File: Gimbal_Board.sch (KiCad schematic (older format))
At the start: 21 parts, among them U1 TM4C129E_Launchpad

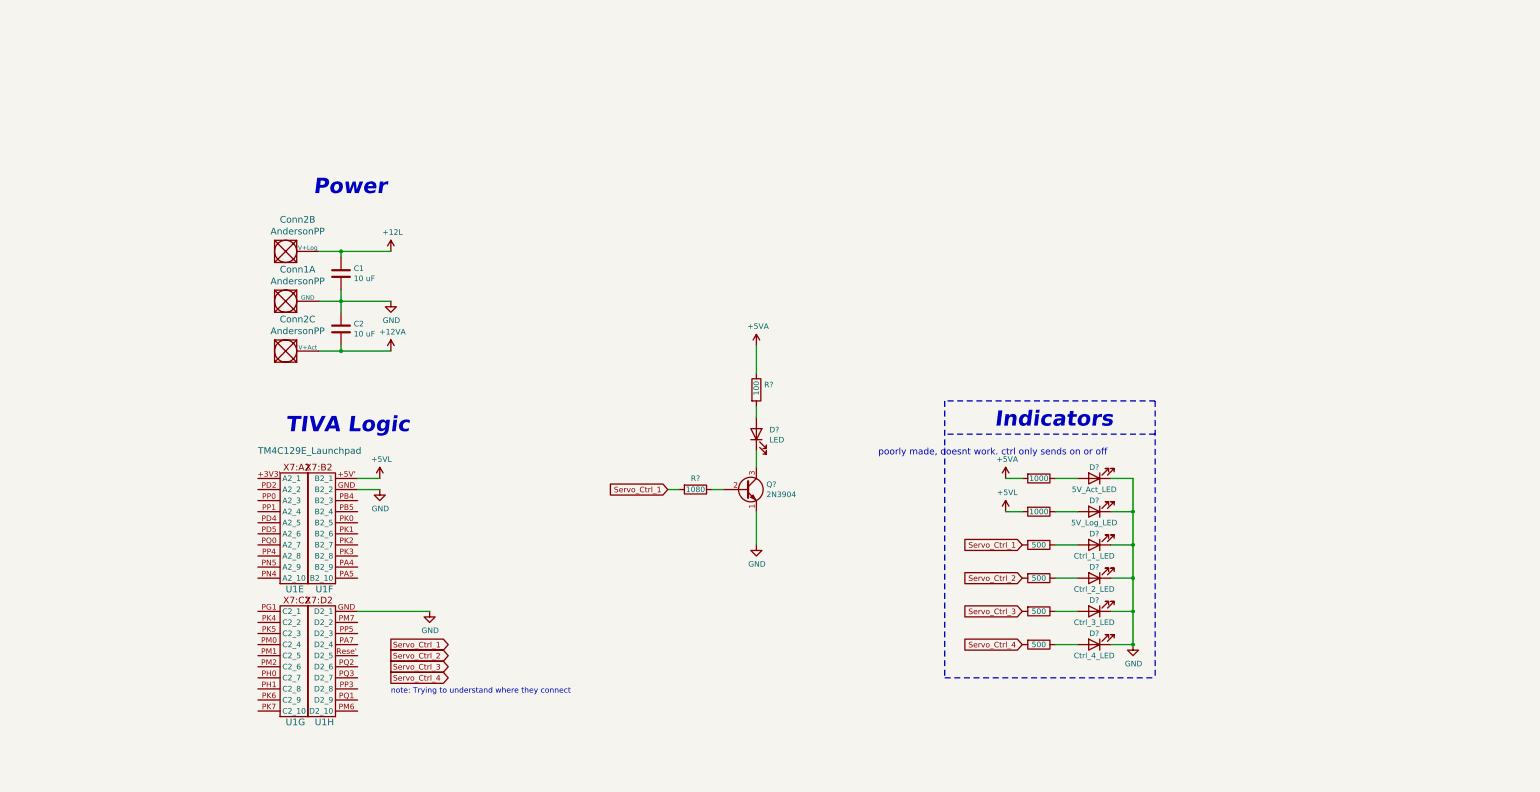
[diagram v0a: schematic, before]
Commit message: Schematic additions
Status of each section is located at the top of the schematic. Added the much of the designs from last year.  Used the updated indicator design (needs to be looked over). Tiva Logic needs to be looked at.
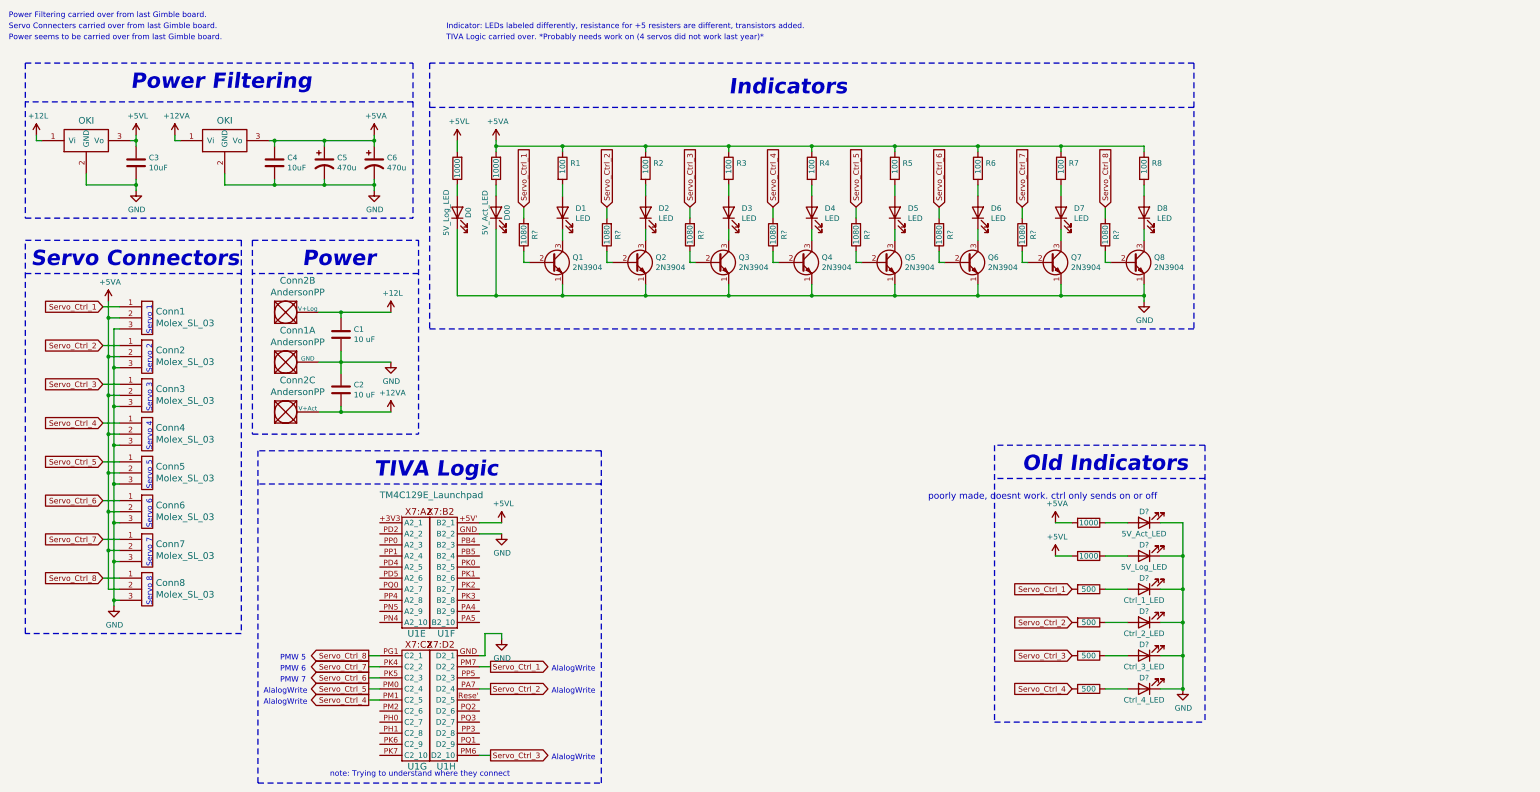
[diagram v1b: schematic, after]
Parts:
- added C3, C4: 10uF, symbol Device:C
- added C5, C6: 470u, symbol Device:CP1
- added Conn1, Conn3, Conn4, Conn5, Conn6, Conn7, Conn8: Molex_SL_03, symbol MRDT_Connectors:Molex_SL_03
- added unit 1 of Conn2
- added D0: 5V_Log_LED, symbol Device:LED
- added D00: 5V_Act_LED, symbol Device:LED
- added D2, D3, D4, D5, D6, D7, D8: LED, symbol Device:LED
- added Q2, Q3, Q4, Q5, Q6, Q7, Q8: 2N3904, Package_TO_SOT_THT:TO-92_Inline, symbol Transistor_BJT:2N3904
- added R2, R3, R4, R5, R6, R7, R8: 100, symbol Device:R
- added R? (x7): 1080, symbol Device:R
- added R? (x2): 1000, symbol Device:R
- added U? (x2): OKI, symbol MRDT_Devices:OKI
- gave numbers to parts that had none: 3
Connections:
- net +12L: now also U?.1 (Vi)
- net +12VA: now also U?.1 (Vi)
- net +5VA: now also C4.1, C5.1, C6.1, Conn1.2, Conn2.2, Conn3.2, Conn4.2, Conn5.2, Conn6.2, Conn7.2, Conn8.2, R2.1, R3.1, R4.1, R5.1, R6.1, R7.1, R8.1, R?.2, U?.3 (Vo)
- net +5VL: now also C3.1, R?.2, U?.3 (Vo)
- net GND: now also C3.2, C4.2, C5.2, C6.2, Conn1.3, Conn2.3, Conn3.3, Conn4.3, Conn5.3, Conn6.3, Conn7.3, Conn8.3, D0.1 (K), D00.1 (K), Q2.1 (E), Q3.1 (E), Q4.1 (E), Q5.1 (E), Q6.1 (E), Q7.1 (E), Q8.1 (E), U?.2 (GND), U?.2 (GND)
- net Servo_Ctrl_1: now also U1.PM7 (D2_2), Conn1.1
- net Servo_Ctrl_2: now also U1.PA7 (D2_4), Conn2.1, R?.2
- net Servo_Ctrl_3: now also U1.PM6 (D2_10), Conn3.1, R?.2
- net Servo_Ctrl_4: now also U1.PM1 (C2_5), Conn4.1, R?.2
- net Servo_Ctrl_8: now reaches U1.PG1 (C2_1)
- net Servo_Ctrl_8: now also Conn8.1, R?.2
- net Servo_Ctrl_7: now reaches U1.PK4 (C2_2)
- net Servo_Ctrl_7: now also Conn7.1, R?.2
- net Servo_Ctrl_6: now reaches U1.PK5 (C2_3)
- net Servo_Ctrl_6: now also Conn6.1, R?.2
- net Servo_Ctrl_5: now reaches U1.PM0 (C2_4)
- net Servo_Ctrl_5: now also Conn5.1, R?.2
- new net: Q2.2 (B), R?.1
- new net: D2.1 (K), Q2.3 (C)
- new net: D2.2 (A), R2.2
- new net: Q3.2 (B), R?.1
- new net: D3.1 (K), Q3.3 (C)
- new net: D3.2 (A), R3.2
- new net: Q4.2 (B), R?.1
- new net: D4.1 (K), Q4.3 (C)
- new net: D4.2 (A), R4.2
- new net: D00.2 (A), R?.1
- new net: D0.2 (A), R?.1
- new net: Q5.2 (B), R?.1
- new net: D5.1 (K), Q5.3 (C)
- new net: D5.2 (A), R5.2
- new net: Q6.2 (B), R?.1
- new net: D6.1 (K), Q6.3 (C)
- new net: D6.2 (A), R6.2
- new net: Q7.2 (B), R?.1
- new net: D7.1 (K), Q7.3 (C)
- new net: D7.2 (A), R7.2
- new net: Q8.2 (B), R?.1
- new net: D8.1 (K), Q8.3 (C)
- new net: D8.2 (A), R8.2
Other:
- note added: "AlalogWrite"
- note added: "Indicator: LEDs labeled differently, resistance for +5 resisters are different, transistors added.\n"
- note added: "Old Indicators"
- note added: "PMW 5"
- note added: "PMW 6"
- note added: "PMW 7"
- note added: "Power Filtering"
- note added: "Power Filtering carried over from last Gimble board."
- note added: "Power seems to be carried over from last Gimble board."
- note added: "Servo 1"
- note added: "Servo 2"
- note added: "Servo 3"
- note added: "Servo 4"
- note added: "Servo 5"
- note added: "Servo 6"
- note added: "Servo 7"
- note added: "Servo 8"
- note added: "Servo Connecters carried over from last Gimble board."
- note added: "Servo Connectors"
- note added: "TIVA Logic carried over. *Probably needs work on (4 servos did not work last year)*"
- moved on the sheet: C1, C2, Conn1A, Conn2B, Conn2C, D1, D?, Q1, R1, R?, U1E, U1F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

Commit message: 6 Servo Changes
Changed to be 6 servos. Pins should be looked over. (Old Indicators should be deleted if no one needs it for reference on this file).
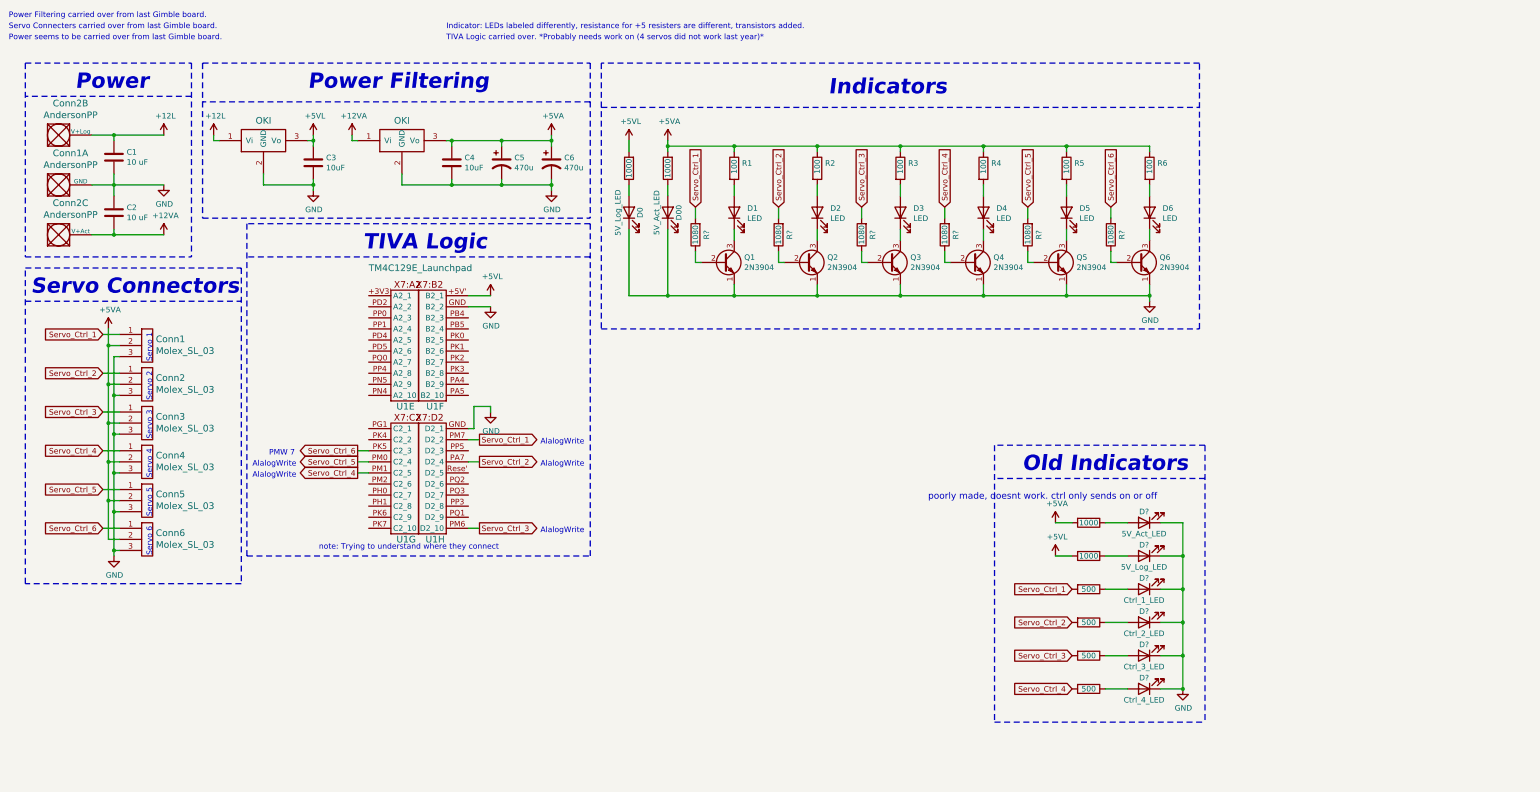
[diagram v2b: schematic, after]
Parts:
- removed Conn7, Conn8: Molex_SL_03, symbol MRDT_Connectors:Molex_SL_03
- removed D7, D8: LED, symbol Device:LED
- removed Q7, Q8: 2N3904, Package_TO_SOT_THT:TO-92_Inline, symbol Transistor_BJT:2N3904
- removed R7, R8: 100, symbol Device:R
- removed R? (x2): 1080, symbol Device:R
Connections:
- net Servo_Ctrl_7: no longer names the net of U1.PK4 (C2_2)
- net Servo_Ctrl_8: no longer names the net of U1.PG1 (C2_1)
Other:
- note removed: "PMW 5"
- note removed: "PMW 6"
- note removed: "Servo 7"
- note removed: "Servo 8"
- moved on the sheet: C1, C2, C3, C4, C5, C6, Conn1, Conn1A, Conn2, Conn2B, Conn2C, Conn3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

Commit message: Added some notes
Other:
- note added: "1000 ohm on servo_ctrl_# would probably suffice"
- note added: "poorly made, doesnt work. ctrl only sends on or off. Not entirely sure why it doesnt work though."
- note removed: "poorly made, doesnt work. ctrl only sends on or off"
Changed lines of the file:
@@
 	9300 4000 9300 6500
 Text Notes 8700 4500 0    59   ~ 0
-poorly made, doesnt work. ctrl only sends on or off
+poorly made, doesnt work. ctrl only sends on or off. Not entirely sure why it doesnt work though.
 Text GLabel 6600 1850 1    50   Input ~ 0
 Servo_Ctrl_1
@@
 	-1   0    0    -1
 $EndComp
+Text Notes 8000 350  0    50   ~ 0
+1000 ohm on servo_ctrl_# would probably suffice
 $EndSCHEMATC

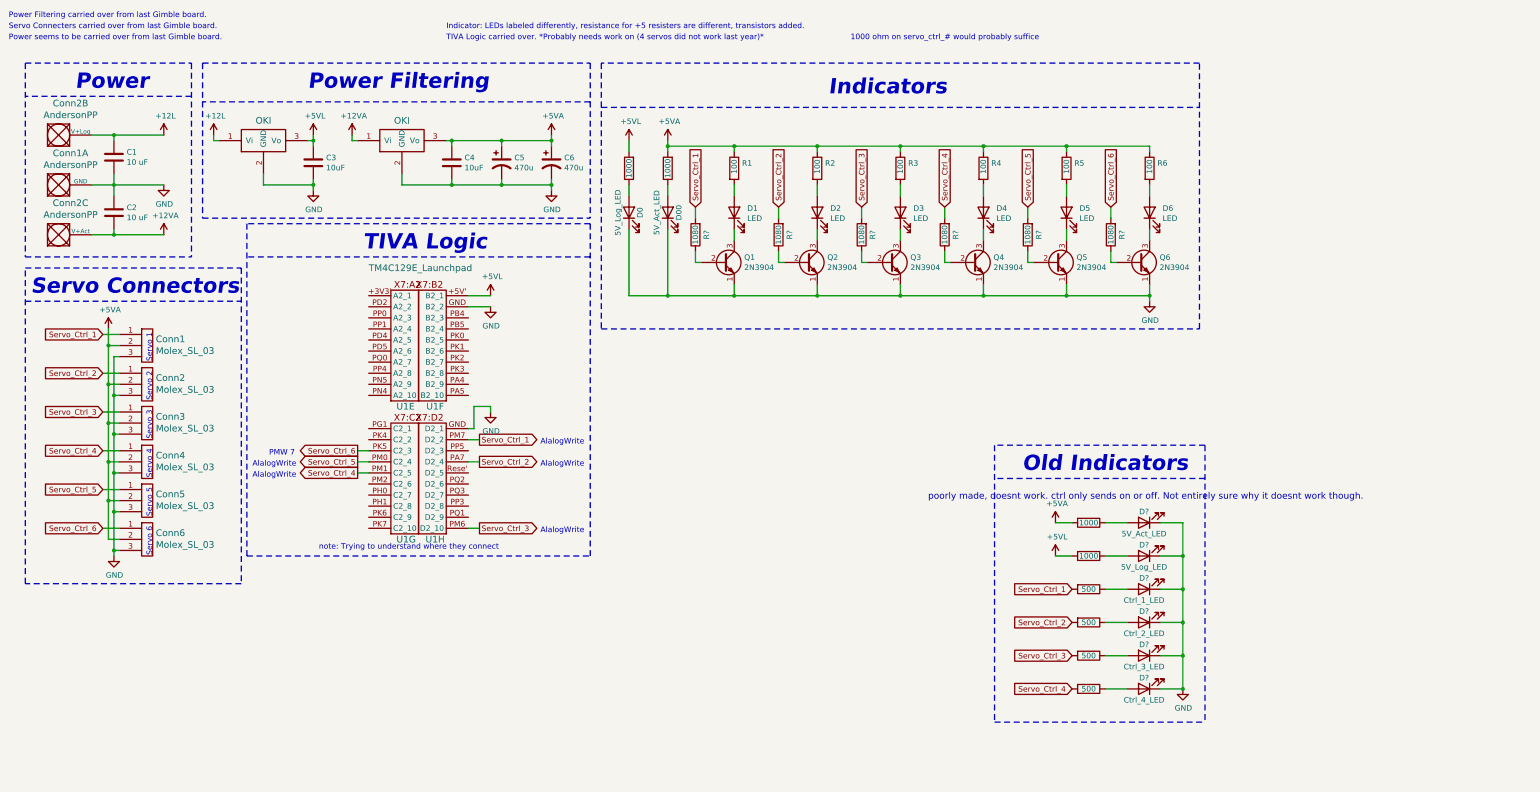
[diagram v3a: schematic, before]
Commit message: Need more servos n such
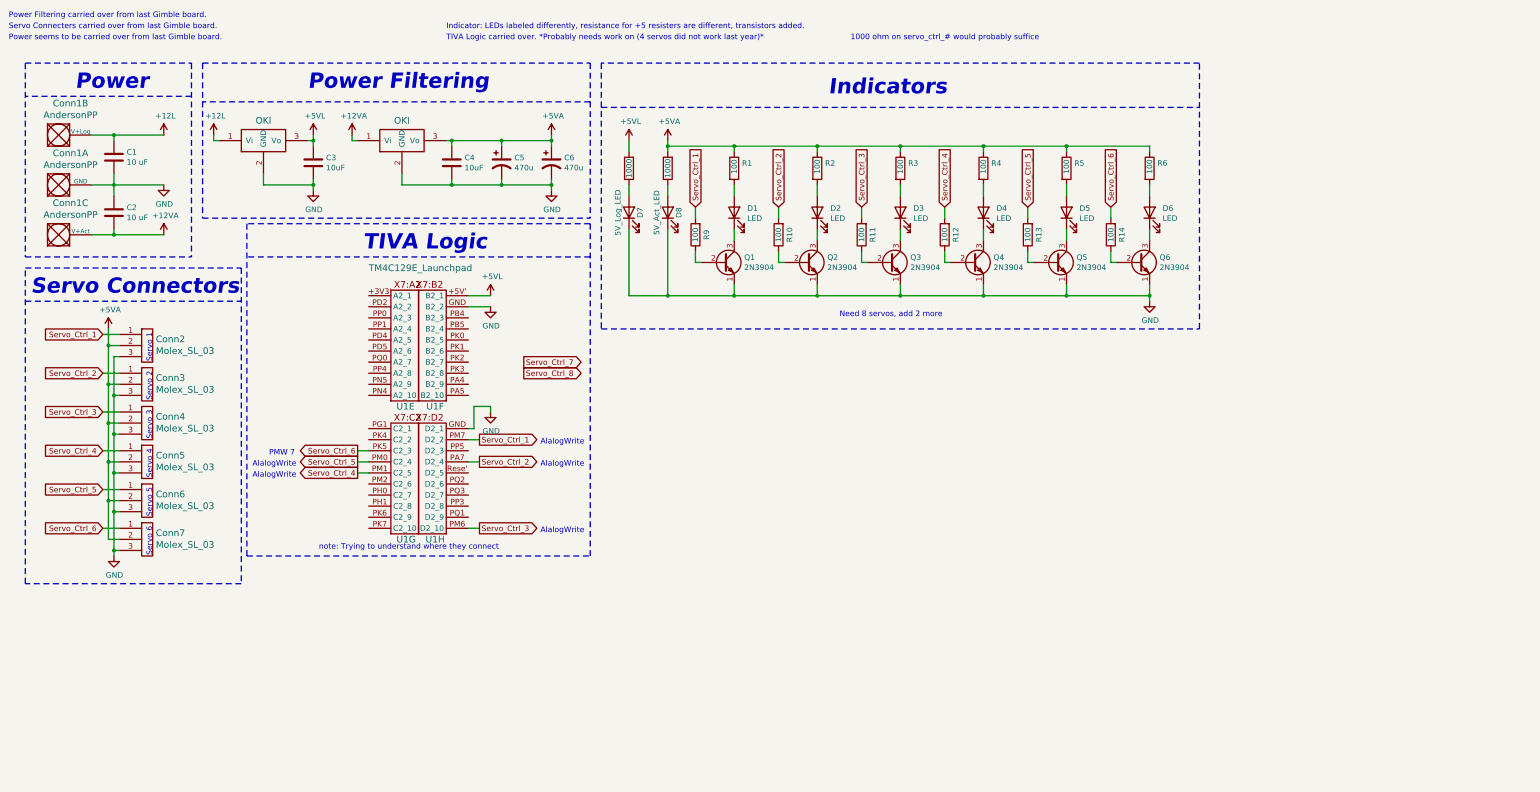
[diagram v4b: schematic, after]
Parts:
- removed D?: 5V_Act_LED, symbol Device:LED
- removed D?: 5V_Log_LED, symbol Device:LED
- removed D?: Ctrl_1_LED, symbol Device:LED
- removed D?: Ctrl_2_LED, symbol Device:LED
- removed D?: Ctrl_3_LED, symbol Device:LED
- removed D?: Ctrl_4_LED, symbol Device:LED
- removed R? (x2): 1000, symbol Device:R
- removed R? (x4): 500, symbol Device:R
- R10, R11, R12, R13, R14, R9: renamed from R?; value 1080 -> 100
- gave numbers to parts that had none: 4
- renumbered Conn2 to Conn1, Conn1 to Conn2, Conn2 to Conn3, Conn3 to Conn4, Conn4 to Conn5, Conn5 to Conn6, Conn6 to Conn7, D0 to D7, D00 to D8
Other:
- note added: "Need 8 servos, add 2 more\n"
- note removed: "Old Indicators"
- note removed: "poorly made, doesnt work. ctrl only sends on or off. Not entirely sure why it doesnt work though."

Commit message: Changed to 8 servo (again)
Added two more servo inputs and relabeled some components.
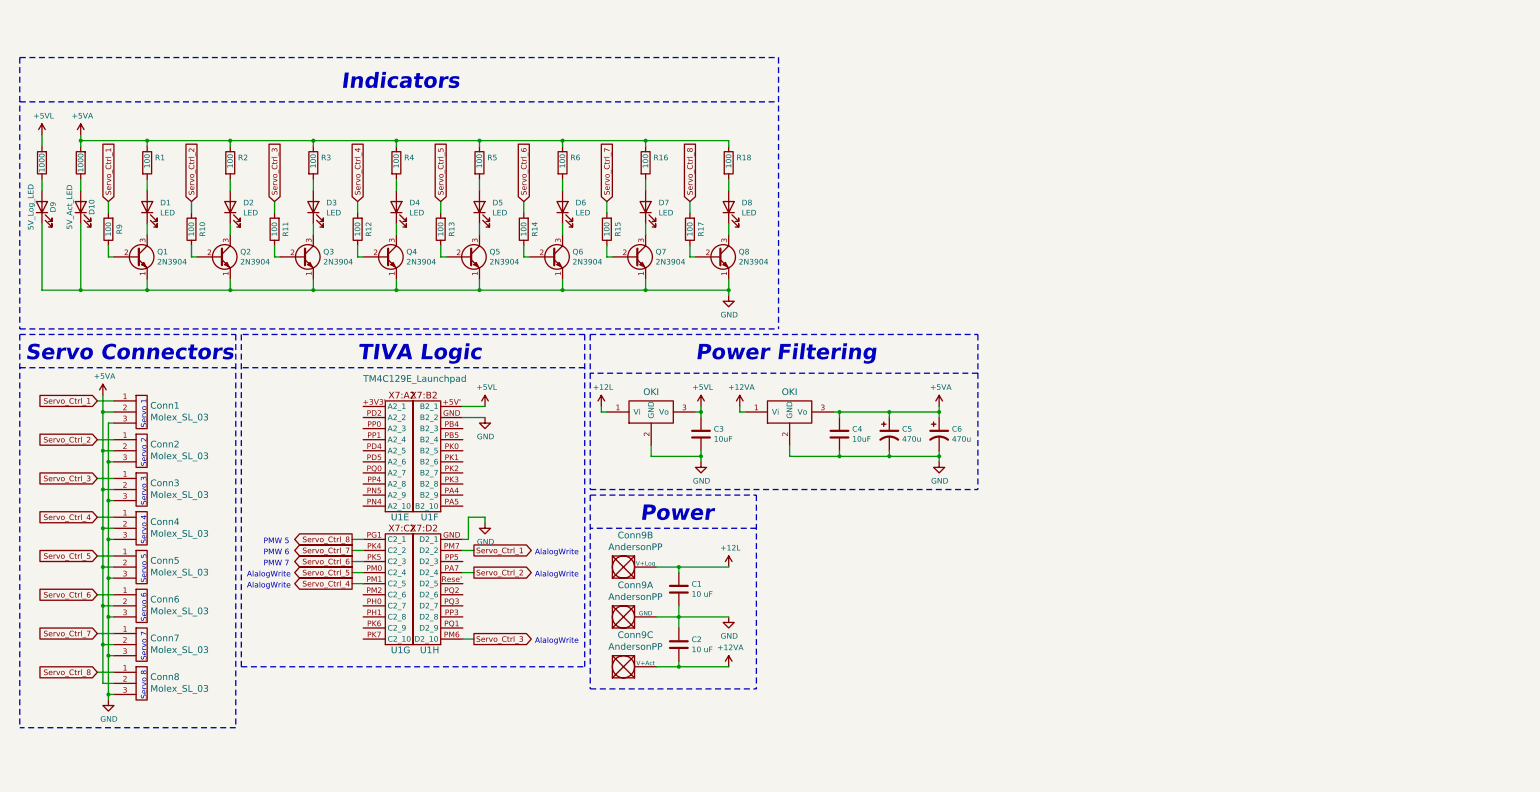
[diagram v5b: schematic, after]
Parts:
- added Conn7, Conn8: Molex_SL_03, symbol MRDT_Connectors:Molex_SL_03
- added D7, D8: LED, symbol Device:LED
- added Q7, Q8: 2N3904, Package_TO_SOT_THT:TO-92_Inline, symbol Transistor_BJT:2N3904
- added R15, R16, R17, R18: 100, symbol Device:R
- renumbered Conn2 to Conn1, Conn3 to Conn2, Conn4 to Conn3, Conn5 to Conn4, Conn6 to Conn5, Conn7 to Conn6, Conn1 to Conn9, D8 to D10, D7 to D9
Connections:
- net +5VA: now also Conn7.2, Conn8.2, R16.1, R18.1
- net GND: now also Conn7.3, Conn8.3, Q7.1 (E), Q8.1 (E)
- net Servo_Ctrl_7: now also U1.PK4 (C2_2), Conn7.1, R15.2
- net Servo_Ctrl_8: now also U1.PG1 (C2_1), Conn8.1, R17.2
- new net: D8.2 (A), R18.2
- new net: D8.1 (K), Q8.3 (C)
- new net: Q8.2 (B), R17.1
- new net: D7.2 (A), R16.2
- new net: D7.1 (K), Q7.3 (C)
- new net: Q7.2 (B), R15.1
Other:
- note added: "PMW 5"
- note added: "PMW 6"
- note added: "Servo 7"
- note added: "Servo 8"
- note removed: "1000 ohm on servo_ctrl_# would probably suffice"
- note removed: "Indicator: LEDs labeled differently, resistance for +5 resisters are different, transistors added.\n"
- note removed: "Need 8 servos, add 2 more\n"
- note removed: "Power Filtering carried over from last Gimble board."
- note removed: "Power seems to be carried over from last Gimble board."
- note removed: "Servo Connecters carried over from last Gimble board."
- note removed: "TIVA Logic carried over. *Probably needs work on (4 servos did not work last year)*"
- note removed: "note: Trying to understand where they connect"
- moved on the sheet: C1, C2, C3, C4, C5, C6, Conn1, Conn2, Conn3, Conn4, Conn5, Conn6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
